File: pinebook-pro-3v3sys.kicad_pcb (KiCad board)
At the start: 2 copper layers, 7.8 x 17.9 mm, 23 parts, among them J1 Conn_01x03, J2 Conn_02x03_Counter_Clockwise, J3 Conn_01x01, J4 Conn_01x03, J5 Conn_01x01, U1 TPS63806

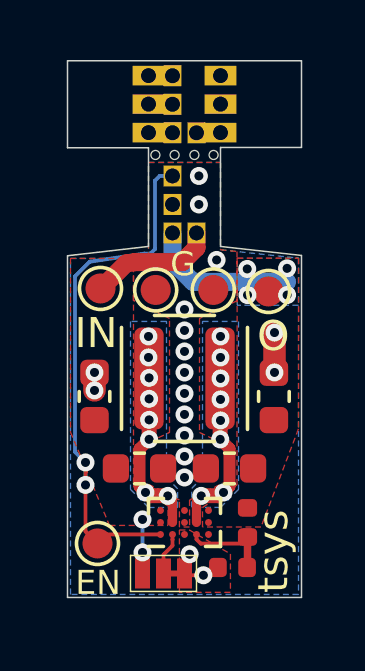
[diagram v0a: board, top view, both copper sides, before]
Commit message: Attach adapter with more supports for easier manufacturing
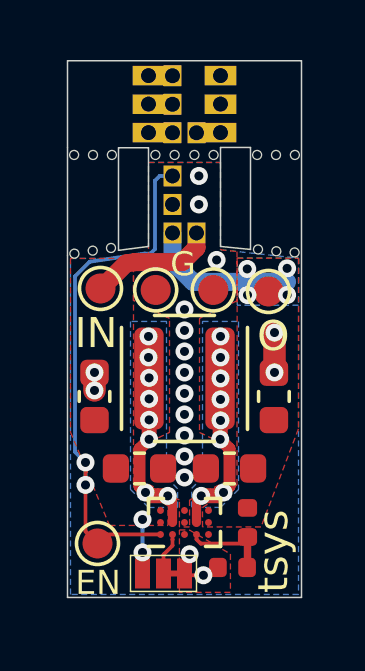
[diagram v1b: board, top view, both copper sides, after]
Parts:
- added H1: MountingHole, Mousebite:Mousebite_0.3mm, F.Cu at (134.1, 52.6)
- added H1: MountingHole, Mousebite:Mousebite_0.3mm, F.Cu at (128.6, 49.4)
- added H1: MountingHole, Mousebite:Mousebite_0.3mm, F.Cu at (128.0, 49.4)
- added H1: MountingHole, Mousebite:Mousebite_0.3mm, F.Cu at (127.3, 49.4)
- added H1: MountingHole, Mousebite:Mousebite_0.3mm, F.Cu at (134.7, 52.6)
- added H1: MountingHole, Mousebite:Mousebite_0.3mm, F.Cu at (133.4, 52.5)
- added H1: MountingHole, Mousebite:Mousebite_0.3mm, F.Cu at (127.3, 52.6)
- added H1: MountingHole, Mousebite:Mousebite_0.3mm, F.Cu at (127.9, 52.5)
- added H1: MountingHole, Mousebite:Mousebite_0.3mm, F.Cu at (128.6, 52.5)
- added H1: MountingHole, Mousebite:Mousebite_0.3mm, F.Cu at (134.7, 49.4)
- added H1: MountingHole, Mousebite:Mousebite_0.3mm, F.Cu at (133.4, 49.4)
- added H1: MountingHole, Mousebite:Mousebite_0.3mm, F.Cu at (134.1, 49.4)
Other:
- outline, holes or cut-outs redrawn
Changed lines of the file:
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@@
-(kicad_pcb (version 20171130) (host pcbnew 5.1.5)
+(kicad_pcb (version 20171130) (host pcbnew 5.1.4)
   (general
     (thickness 1.6)
-    (drawings 26)
+    (drawings 28)
     (tracks 122)
     (zones 0)
-    (modules 23)
+    (modules 35)
     (nets 16)
   )
@@
     (add_net VIN)
   )
+  (module Mousebite:Mousebite_0.3mm (layer F.Cu)
+    (at 134.06 52.56 180)
+    (fp_text reference H1 (at 0 0.5) (layer F.SilkS) hide
+      (effects (font (size 1 1) (thickness 0.15)))
+    )
+    (fp_text value MountingHole (at 0 -0.5) (layer F.Fab) hide
+      (effects (font (size 1 1) (thickness 0.15)))
+    )
+    (pad "" np_thru_hole circle (at 0 0 180) (size 0.3 0.3) (drill 0.3) (layers *.Cu *.Mask))
+  )
+  (module Mousebite:Mousebite_0.3mm (layer F.Cu)
+    (at 134.67 52.6 180)
+    (fp_text reference H1 (at 0 0.5) (layer F.SilkS) hide
+      (effects (font (size 1 1) (thickness 0.15)))
+    )
+    (fp_text value MountingHole (at 0 -0.5) (layer F.Fab) hide
+      (effects (font (size 1 1) (thickness 0.15)))
+    )
+    (pad "" np_thru_hole circle (at 0 0 180) (size 0.3 0.3) (drill 0.3) (layers *.Cu *.Mask))
+  )
+  (module Mousebite:Mousebite_0.3mm (layer F.Cu)
+    (at 133.45 52.5 180)
+    (fp_text reference H1 (at 0 0.5) (layer F.SilkS) hide
+      (effects (font (size 1 1) (thickness 0.15)))
+    )
+    (fp_text value MountingHole (at 0 -0.5) (layer F.Fab) hide
+      (effects (font (size 1 1) (thickness 0.15)))
+    )
+    (pad "" np_thru_hole circle (at 0 0 180) (size 0.3 0.3) (drill 0.3) (layers *.Cu *.Mask))
+  )
+  (module Mousebite:Mousebite_0.3mm (layer F.Cu)
+    (at 127.33 52.64)
+    (fp_text reference H1 (at 0 0.5) (layer F.SilkS) hide
+      (effects (font (size 1 1) (thickness 0.15)))
+    )
+    (fp_text value MountingHole (at 0 -0.5) (layer F.Fab) hide
+      (effects (font (size 1 1) (thickness 0.15)))
+    )
+    (pad "" np_thru_hole circle (at 0 0) (size 0.3 0.3) (drill 0.3) (layers *.Cu *.Mask))
+  )
+  (module Mousebite:Mousebite_0.3mm (layer F.Cu)
+    (at 127.94 52.54)
+    (fp_text reference H1 (at 0 0.5) (layer F.SilkS) hide
+      (effects (font (size 1 1) (thickness 0.15)))
+    )
+    (fp_text value MountingHole (at 0 -0.5) (layer F.Fab) hide
+      (effects (font (size 1 1) (thickness 0.15)))
+    )
+    (pad "" np_thru_hole circle (at 0 0) (size 0.3 0.3) (drill 0.3) (layers *.Cu *.Mask))
+  )
+  (module Mousebite:Mousebite_0.3mm (layer F.Cu)
+    (at 128.55 52.45)
+    (fp_text reference H1 (at 0 0.5) (layer F.SilkS) hide
+      (effects (font (size 1 1) (thickness 0.15)))
+    )
+    (fp_text value MountingHole (at 0 -0.5) (layer F.Fab) hide
+      (effects (font (size 1 1) (thickness 0.15)))
+    )
+    (pad "" np_thru_hole circle (at 0 0) (size 0.3 0.3) (drill 0.3) (layers *.Cu *.Mask))
+  )
+  (module Mousebite:Mousebite_0.3mm (layer F.Cu)
+    (at 134.68 49.35 180)
+    (fp_text reference H1 (at 0 0.5) (layer F.SilkS) hide
+      (effects (font (size 1 1) (thickness 0.15)))
+    )
+    (fp_text value MountingHole (at 0 -0.5) (layer F.Fab) hide
+      (effects (font (size 1 1) (thickness 0.15)))
+    )
+    (pad "" np_thru_hole circle (at 0 0 180) (size 0.3 0.3) (drill 0.3) (layers *.Cu *.Mask))
+  )
+  (module Mousebite:Mousebite_0.3mm (layer F.Cu)
+    (at 133.42 49.35 180)
+    (fp_text reference H1 (at 0 0.5) (layer F.SilkS) hide
+      (effects (font (size 1 1) (thickness 0.15)))
+    )
+    (fp_text value MountingHole (at 0 -0.5) (layer F.Fab) hide
+      (effects (font (size 1 1) (thickness 0.15)))
+    )
+    (pad "" np_thru_hole circle (at 0 0 180) (size 0.3 0.3) (drill 0.3) (layers *.Cu *.Mask))
+  )
+  (module Mousebite:Mousebite_0.3mm (layer F.Cu)
+    (at 134.05 49.35 180)
+    (fp_text reference H1 (at 0 0.5) (layer F.SilkS) hide
+      (effects (font (size 1 1) (thickness 0.15)))
+    )
+    (fp_text value MountingHole (at 0 -0.5) (layer F.Fab) hide
+      (effects (font (size 1 1) (thickness 0.15)))
+    )
+    (pad "" np_thru_hole circle (at 0 0 180) (size 0.3 0.3) (drill 0.3) (layers *.Cu *.Mask))
+  )
+  (module Mousebite:Mousebite_0.3mm (layer F.Cu)
+    (at 128.58 49.35)
+    (fp_text reference H1 (at 0 0.5) (layer F.SilkS) hide
+      (effects (font (size 1 1) (thickness 0.15)))
+    )
+    (fp_text value MountingHole (at 0 -0.5) (layer F.Fab) hide
+      (effects (font (size 1 1) (thickness 0.15)))
+    )
+    (pad "" np_thru_hole circle (at 0 0) (size 0.3 0.3) (drill 0.3) (layers *.Cu *.Mask))
+  )
+  (module Mousebite:Mousebite_0.3mm (layer F.Cu)
+    (at 127.95 49.35)
+    (fp_text reference H1 (at 0 0.5) (layer F.SilkS) hide
+      (effects (font (size 1 1) (thickness 0.15)))
+    )
+    (fp_text value MountingHole (at 0 -0.5) (layer F.Fab) hide
+      (effects (font (size 1 1) (thickness 0.15)))
+    )
+    (pad "" np_thru_hole circle (at 0 0) (size 0.3 0.3) (drill 0.3) (layers *.Cu *.Mask))
+  )
+  (module Mousebite:Mousebite_0.3mm (layer F.Cu)
+    (at 127.32 49.35)
+    (fp_text reference H1 (at 0 0.5) (layer F.SilkS) hide
+      (effects (font (size 1 1) (thickness 0.15)))
+    )
+    (fp_text value MountingHole (at 0 -0.5) (layer F.Fab) hide
+      (effects (font (size 1 1) (thickness 0.15)))
+    )
+    (pad "" np_thru_hole circle (at 0 0) (size 0.3 0.3) (drill 0.3) (layers *.Cu *.Mask))
+  )
   (module Package_DSBGA:DSBGA-15-P0.4mm (layer F.Cu)
     (at 131 61.6 90)
@@
     )
   )
+  (gr_line (start 128.8 52.53) (end 128.8 49.11) (layer Edge.Cuts) (width 0.05))
+  (gr_line (start 133.2 52.5) (end 133.2 49.1) (layer Edge.Cuts) (width 0.05))
+  (gr_line (start 127.1 49.11) (end 127.1 52.71) (layer Edge.Cuts) (width 0.05))
   (gr_text "Rev A" (at 134.06 57.28 270) (layer B.SilkS)
     (effects (font (size 0.8 0.8) (thickness 0.15)) (justify mirror))
@@
     (effects (font (size 0.8 0.8) (thickness 0.15)) (justify mirror))
   )
-  (gr_line (start 134.9 49.1) (end 132.2 49.1) (layer Edge.Cuts) (width 0.05))
+  (gr_line (start 133.2 49.1) (end 132.2 49.1) (layer Edge.Cuts) (width 0.05))
   (gr_line (start 128.75 49.5) (end 133.45 49.5) (layer F.Fab) (width 0.05))
   (dimension 7.8 (width 0.15) (layer Eco1.User)
@@
   )
   (gr_line (start 131 49) (end 131 53.1) (layer F.Fab) (width 0.05))
-  (gr_line (start 132.2 52.4) (end 134.9 52.7) (layer Edge.Cuts) (width 0.05))
+  (gr_line (start 132.2 52.4) (end 133.2 52.5) (layer Edge.Cuts) (width 0.05))
   (gr_line (start 132.2 49.1) (end 132.2 52.4) (layer Edge.Cuts) (width 0.05))
   (gr_line (start 129.8 52.4) (end 129.8 49.11) (layer Edge.Cuts) (width 0.05))
-  (gr_line (start 127.1 52.71) (end 129.8 52.4) (layer Edge.Cuts) (width 0.05))
+  (gr_line (start 128.8 52.53) (end 129.8 52.4) (layer Edge.Cuts) (width 0.05))
   (gr_line (start 127.1 64.1) (end 127.1 52.71) (layer Edge.Cuts) (width 0.05))
   (gr_line (start 134.9 64.1) (end 127.1 64.1) (layer Edge.Cuts) (width 0.05))
-  (gr_line (start 134.9 52.7) (end 134.9 64.1) (layer Edge.Cuts) (width 0.05))
+  (gr_line (start 134.9 46.21) (end 134.9 64.1) (layer Edge.Cuts) (width 0.05))
   (gr_line (start 127.1 49.11) (end 127.1 46.21) (layer Edge.Cuts) (width 0.05))
-  (gr_line (start 129.8 49.11) (end 127.1 49.11) (layer Edge.Cuts) (width 0.05))
-  (gr_line (start 134.9 46.21) (end 134.9 49.1) (layer Edge.Cuts) (width 0.05))
+  (gr_line (start 129.8 49.11) (end 128.8 49.11) (layer Edge.Cuts) (width 0.05))
   (gr_line (start 127.1 46.21) (end 134.9 46.21) (layer Edge.Cuts) (width 0.05))
   (via (at 128 56.6) (size 0.6) (drill 0.3) (layers F.Cu B.Cu) (net 1))
